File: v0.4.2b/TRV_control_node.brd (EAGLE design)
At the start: 65 x 30.7 mm, 47 parts, among them J3 AMP FCI 10103594-0001LF, J4 455-1750-1-ND, J6 AMP FCI 10103594-0001LF, SW1 EVQQ, SW2 EVQQ, U1 PCA9306, U11 915MHz, U2 FT231XQ-R, U5 ATMEGA328P-MU, U8 MCP1703/3.3V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

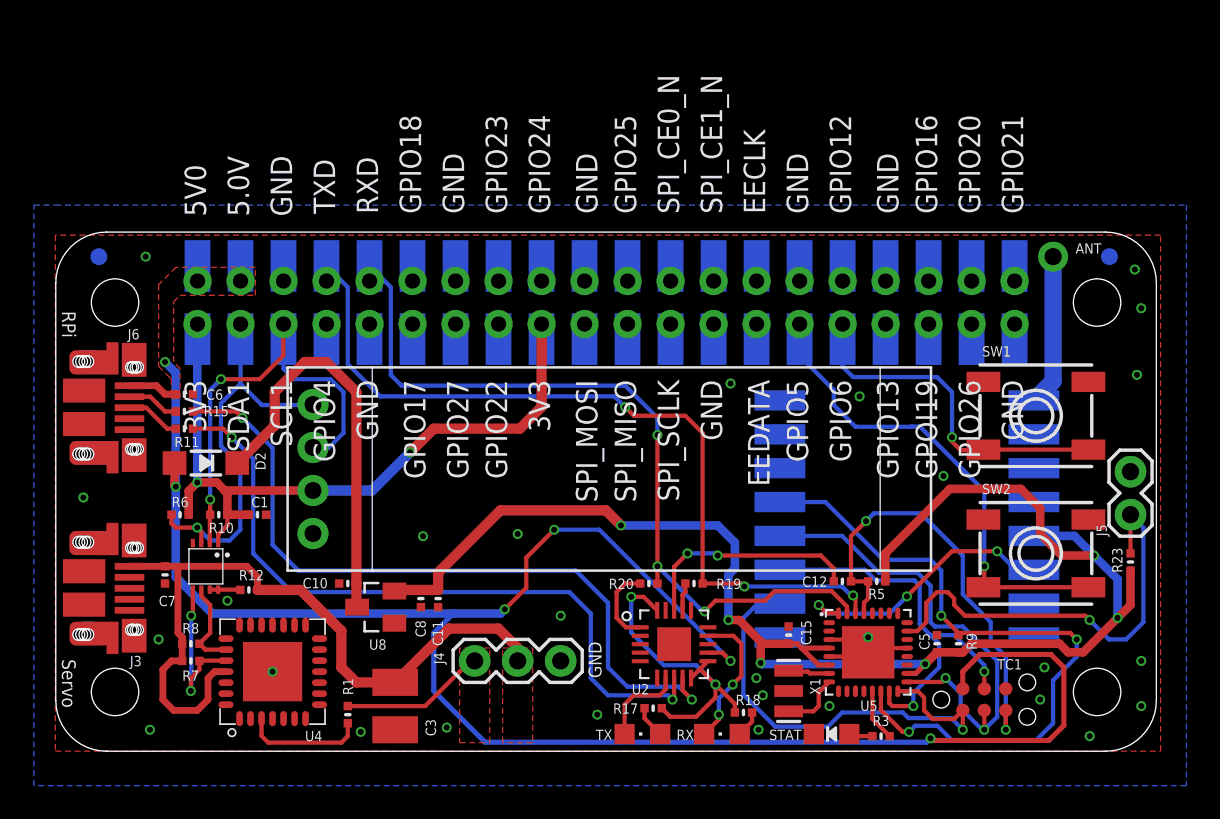
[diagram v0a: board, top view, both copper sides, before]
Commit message: v0.4.2b & v0.4.3 - proper versioning & update
- Renamed v0.4.3 to v0.4.2b -- this design is not used as some parts are physically "moved" on the board.
- v0.4.3 - this design now incorporates the following:
- thermistor header pins for extra temperature monitoring if needed
- Relocation of antenna hole away from buttons
- Added SMD pads for servo
- silkscreen update
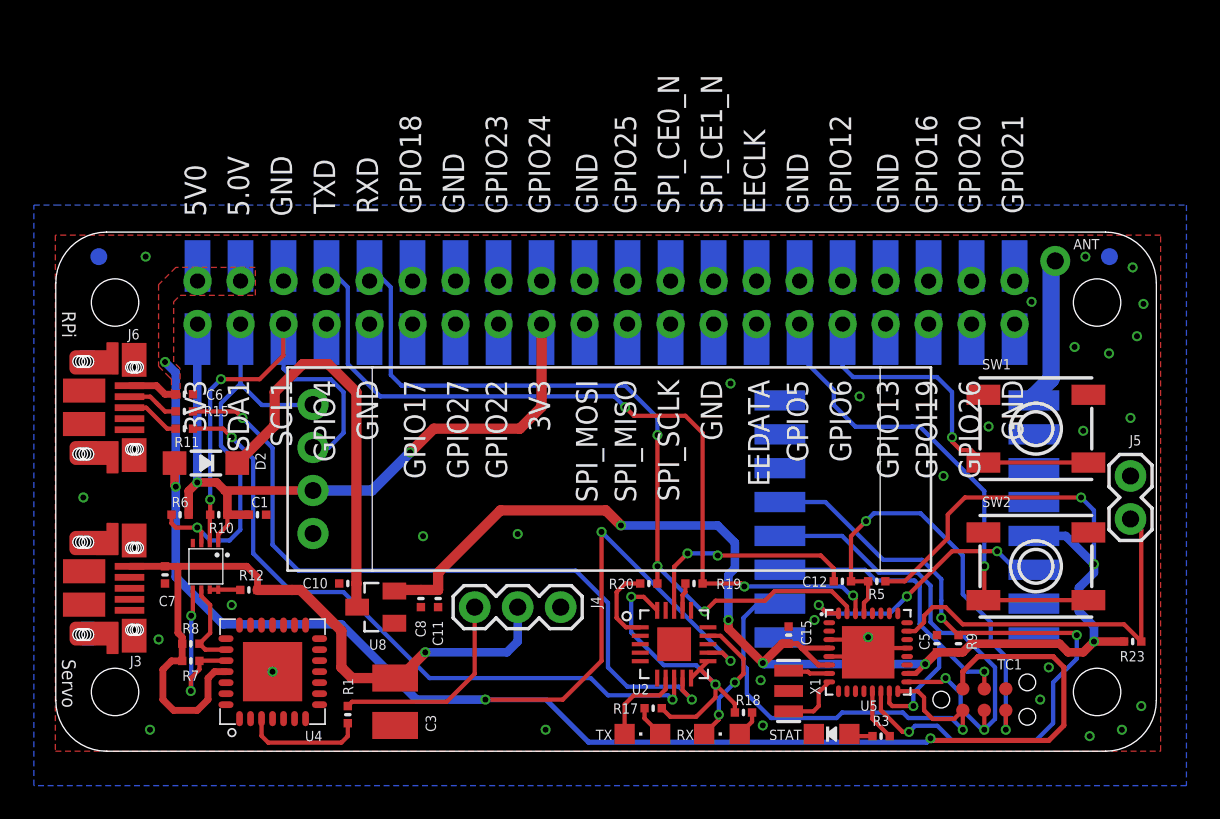
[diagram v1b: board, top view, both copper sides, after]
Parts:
- moved R23 4.70 mm to (63.6, 6.48), turned to 0 degrees
- moved J4 3.18 mm to (29.8, 8.51)
- moved SW1 0.76 mm to (57.9, 19.1)
- moved SW2 0.76 mm to (57.9, 10.9)
- moved ANT 0.28 mm to (59.1, 29.0)
- moved J5 0.25 mm to (63.5, 13.7)
- moved C3 0.25 mm to (20.1, 2.92)
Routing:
- net CH0: track 8.60 -> 12.2 mm
- net A0: track 26.3 -> 23.0 mm, vias 1 -> 0
- net N$26: track 41.8 -> 39.5 mm
- net VCC: track 91.6 -> 90.1 mm, vias 6 -> 7
- net MOSI: track 24.4 -> 23.4 mm
- net 5VA: track 115.8 -> 114.9 mm
- net GPIO5: track 28.5 -> 29.3 mm
- net MISO: track 27.9 -> 27.4 mm
- net 5VB: track 44.5 -> 44.8 mm, vias 0 -> 1
- net GND: vias 28 -> 31
- removed copper zone on layer 1, net 5VB
- removed copper zone on layer 1, net CH0
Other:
- board text added: "TRV Control Node v0.4.3 August 2018"
- board text removed: "GND"
- board text removed: "TRV Control Node v0.4.3 September 2018"
